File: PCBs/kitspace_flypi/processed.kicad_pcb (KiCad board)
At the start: 2 copper layers, 57.2 x 146.6 mm, 53 parts, among them J1 USB_A, P1 PeltS1S2, P10 RGB RG-B, P3 Fan+-, P4 Therm +s-, P5 HP1+-, P6 HP2+-, P7 servo +s-, P8 Ring +-s, P9 matrix +-sdsc, Q1 1A_NPN_ECB, Q2 1A-NPN-ECB, Q3 1A_NPN_ECB, Q4 1A_NPN_ECB, U1 LM2596S-5, U2 LM2596S-5, U3 LM2596S-5

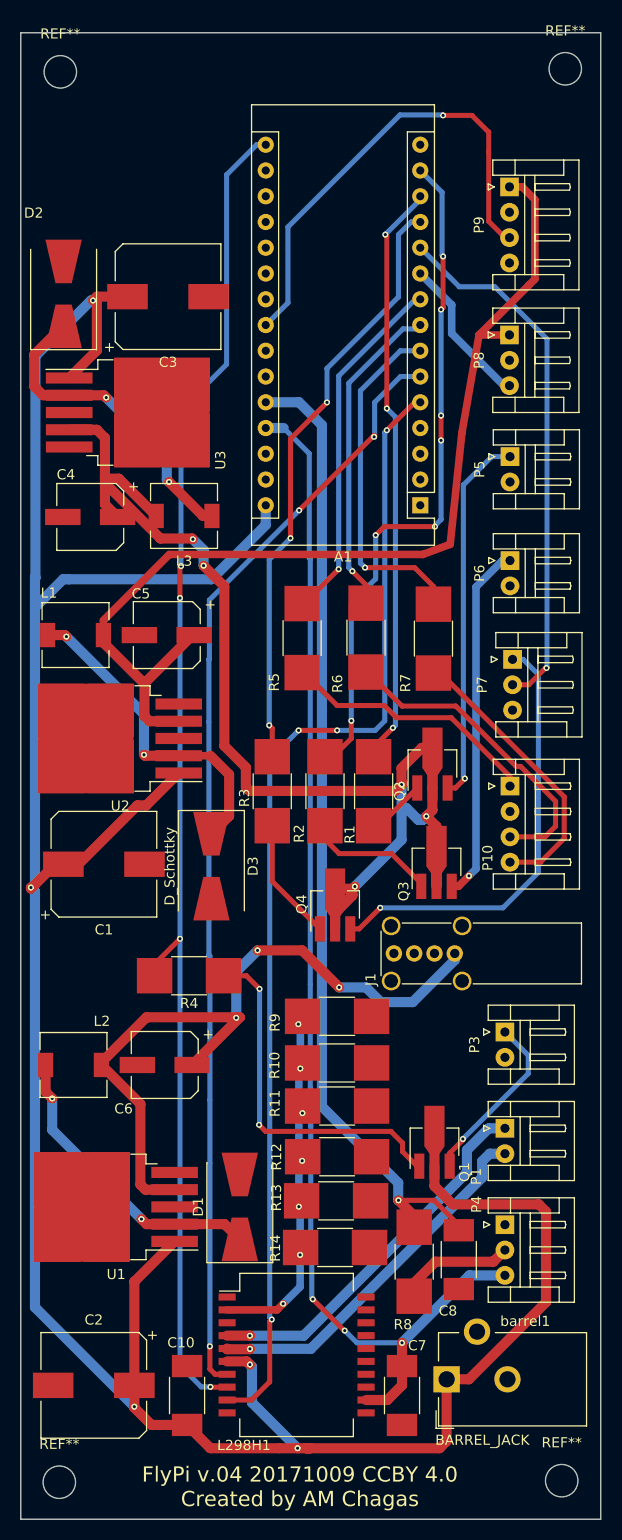
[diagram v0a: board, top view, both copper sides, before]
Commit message: recheck all circuits and clean up fill zone by rerouting the nets using freerouting and manually
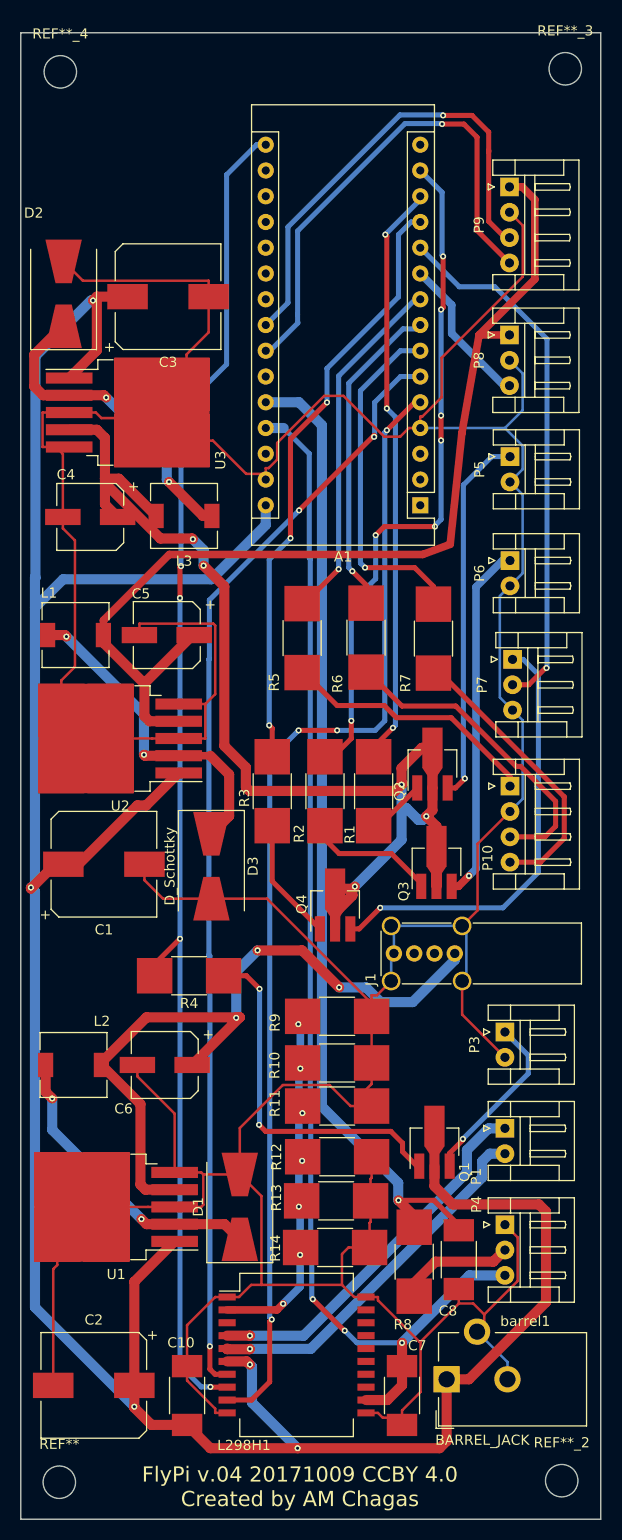
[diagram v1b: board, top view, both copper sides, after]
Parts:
- renumbered REF** to REF**_2, REF** to REF**_3, REF** to REF**_4
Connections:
- A1 pad 1: (no net) -> Net-(A1-Pad1)
- A1 pad 15: (no net) -> Net-(A1-Pad15)
- A1 pad 17: (no net) -> Net-(A1-Pad17)
- A1 pad 18: (no net) -> Net-(A1-Pad18)
- A1 pad 19: (no net) -> Net-(A1-Pad19)
- A1 pad 2: (no net) -> Net-(A1-Pad2)
- A1 pad 20: (no net) -> Net-(A1-Pad20)
- A1 pad 21: (no net) -> Net-(A1-Pad21)
- A1 pad 22: (no net) -> Net-(A1-Pad22)
- A1 pad 24: (no net) -> Net-(A1-Pad24)
- A1 pad 25: (no net) -> Net-(A1-Pad25)
- A1 pad 28: (no net) -> Net-(A1-Pad28)
- A1 pad 29: (no net) -> GND
- A1 pad 3: (no net) -> Net-(A1-Pad3)
- A1 pad 4: (no net) -> GND
- C1 pad 2: (no net) -> GND
- C10 pad 1: (no net) -> GND
- C2 pad 2: (no net) -> GND
- C3 pad 2: (no net) -> GND
- C4 pad 2: (no net) -> GND
- C5 pad 2: (no net) -> GND
- C6 pad 2: (no net) -> GND
- C7 pad 2: (no net) -> GND
- C8 pad 1: (no net) -> GND
- D1 pad 2: (no net) -> GND
- D2 pad 2: (no net) -> GND
- D3 pad 2: (no net) -> GND
- J1 pad 2: (no net) -> Net-(J1-Pad2)
- J1 pad 3: (no net) -> Net-(J1-Pad3)
- J1 pad 4: (no net) -> GND
- J1 pad 5: (no net) -> GND
- L298H1 pad 1: (no net) -> GND
- L298H1 pad 10: (no net) -> GND
- L298H1 pad 11: (no net) -> GND
- L298H1 pad 13: (no net) -> Net-(L298H1-Pad13)
- L298H1 pad 14: (no net) -> Net-(L298H1-Pad14)
- L298H1 pad 15: (no net) -> Net-(L298H1-Pad15)
- L298H1 pad 16: (no net) -> Net-(L298H1-Pad16)
- L298H1 pad 17: (no net) -> Net-(L298H1-Pad17)
- L298H1 pad 18: (no net) -> Net-(L298H1-Pad18)
- L298H1 pad 19: (no net) -> Net-(L298H1-Pad19)
- L298H1 pad 20: (no net) -> GND
- L298H1 pad 3: (no net) -> Net-(L298H1-Pad3)
- P10 pad 2: (no net) -> GND
- P3 pad 2: (no net) -> GND
- P4 pad 1: (no net) -> GND
- P5 pad 2: (no net) -> GND
- P6 pad 2: (no net) -> GND
- P7 pad 3: (no net) -> GND
- P8 pad 2: (no net) -> GND
- P9 pad 2: (no net) -> GND
- P9 pad 4: (no net) -> Net-(A1-Pad24)
- R10 pad 1: (no net) -> GND
- R11 pad 1: (no net) -> GND
- R12 pad 1: (no net) -> GND
- R13 pad 1: (no net) -> GND
- R14 pad 1: (no net) -> GND
- R9 pad 1: (no net) -> GND
- U1 pad 3: (no net) -> GND
- U1 pad 5: (no net) -> GND
- U2 pad 3: (no net) -> GND
- U2 pad 5: (no net) -> GND
- U3 pad 3: (no net) -> GND
- U3 pad 5: (no net) -> GND
- barrel1 pad 2: (no net) -> GND
- barrel1 pad 3: (no net) -> GND
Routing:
- net GND: track 0.00 -> 521.2 mm
- net Net-(A1-Pad24): track 0.00 -> 50.6 mm, vias 0 -> 1
- net Net-(A1-Pad30): track 290.7 -> 289.7 mm
- net Net-(C5-Pad1): track 101.2 -> 101.7 mm
